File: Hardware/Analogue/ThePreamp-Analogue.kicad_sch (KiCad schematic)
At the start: 32 parts, among them IC1 ULN2803CDWR, J1 To preamp, J14 Conn_01x03_Pin, J15 Switch & trigger outputs and 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, J2 From preamp, J3 Digital In, J4 Digital Pass Through, J5 Power In, J6 Power Out, J7 ADS1115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

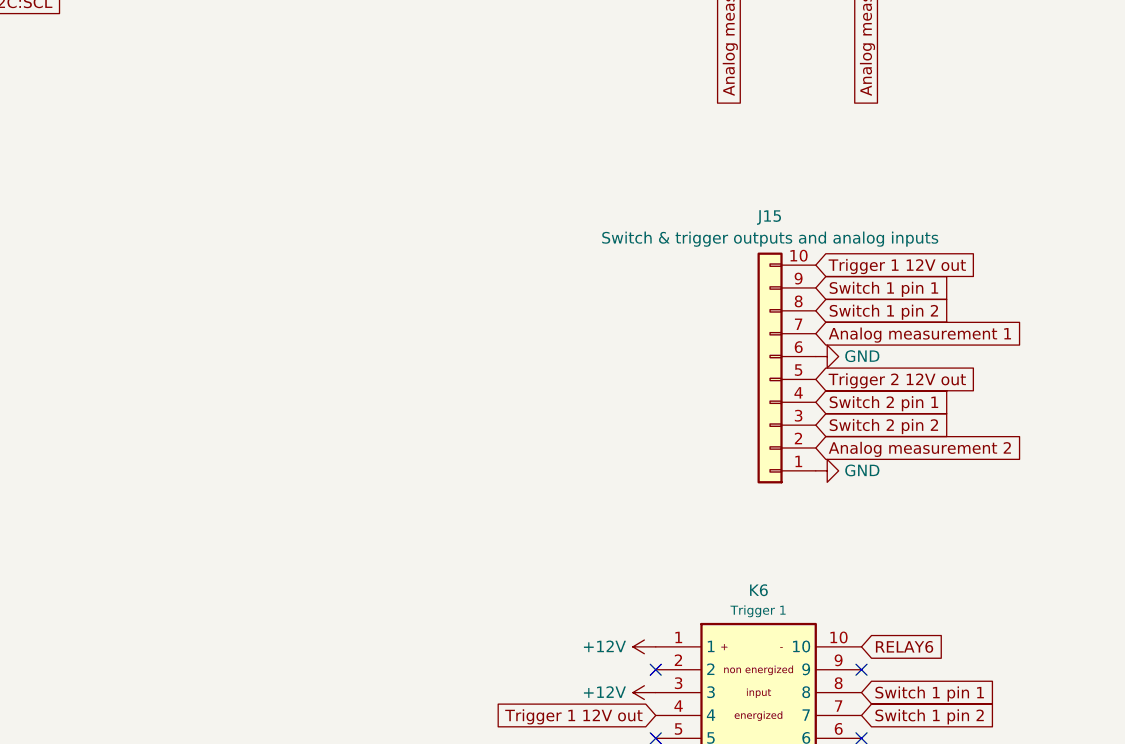
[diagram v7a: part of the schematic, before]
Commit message: Added optional M8 connectors for switches, 12V triggers and analog measurements
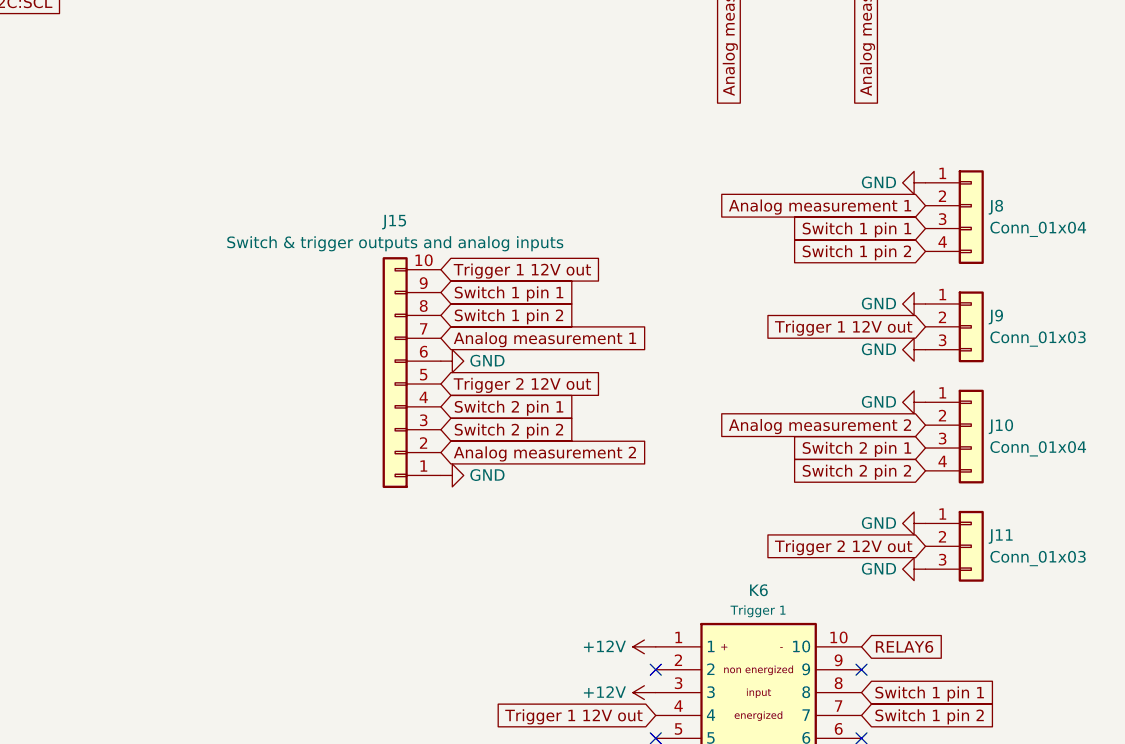
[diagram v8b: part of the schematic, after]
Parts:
- added J10, J8: Conn_01x04, Connector_M8:M8 4 pin, symbol Connector_Generic:Conn_01x04
- added J11, J9: Conn_01x03, Connector_M8:M8 3 pin, symbol Connector_Generic:Conn_01x03
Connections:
- net A0: now also J8.2 (Pin_2)
- net A1: now also J10.2 (Pin_2)
- net GND: now also J10.1 (Pin_1), J11.1 (Pin_1), J11.3 (Pin_3), J8.1 (Pin_1), J9.1 (Pin_1), J9.3 (Pin_3)
- net Switch 1 pin 1: now also J8.3 (Pin_3)
- net Switch 1 pin 2: now also J8.4 (Pin_4)
- net Switch 2 pin 1: now also J10.3 (Pin_3)
- net Switch 2 pin 2: now also J10.4 (Pin_4)
- net Trigger 1 12V out: now also J9.2 (Pin_2)
- net Trigger 2 12V out: now also J11.2 (Pin_2)
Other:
- moved on the sheet: J15
